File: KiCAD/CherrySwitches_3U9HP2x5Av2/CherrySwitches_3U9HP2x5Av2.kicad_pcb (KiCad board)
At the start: 2 copper layers, 45.4 x 128.5 mm, 14 parts, among them SW1 SW_SPST_MOUNT, SW10 SW_SPST_MOUNT, SW2 SW_SPST_MOUNT, SW3 SW_SPST_MOUNT, SW4 SW_SPST_MOUNT, SW5 SW_SPST_MOUNT, SW6 SW_SPST_MOUNT, SW7 SW_SPST_MOUNT, SW8 SW_SPST_MOUNT, SW9 SW_SPST_MOUNT

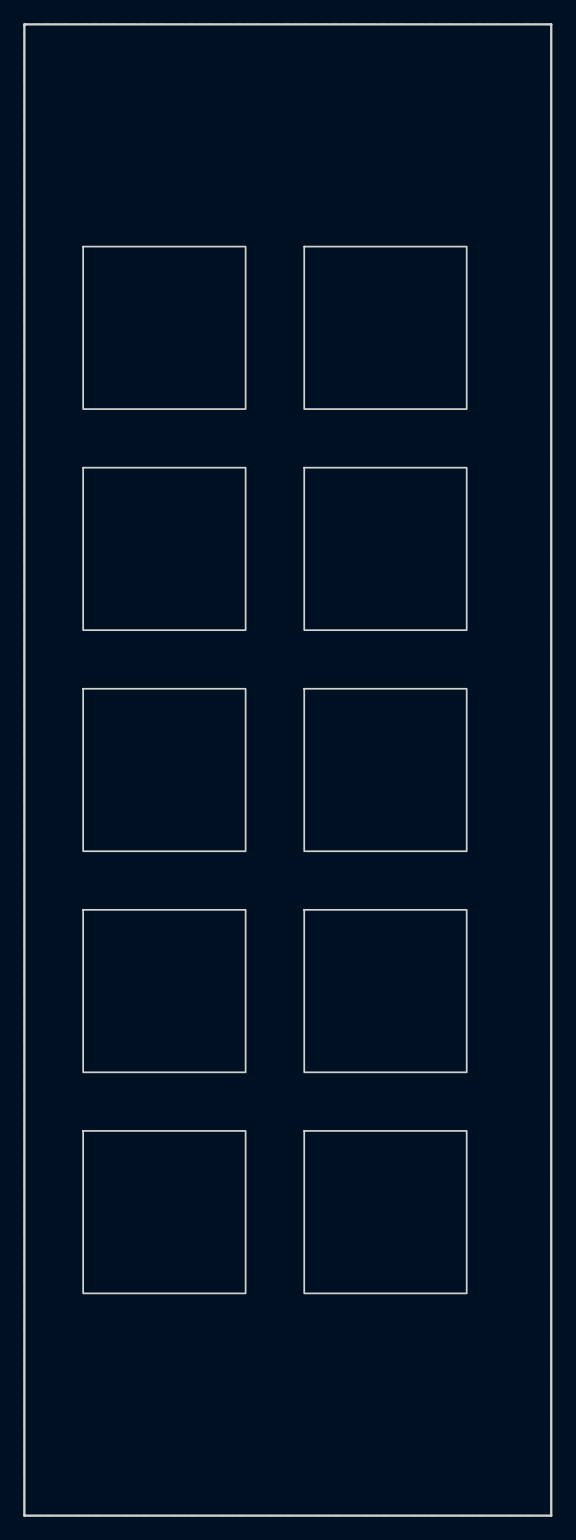
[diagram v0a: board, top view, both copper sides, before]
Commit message: updated all modules to use plated through-holes wherever possible
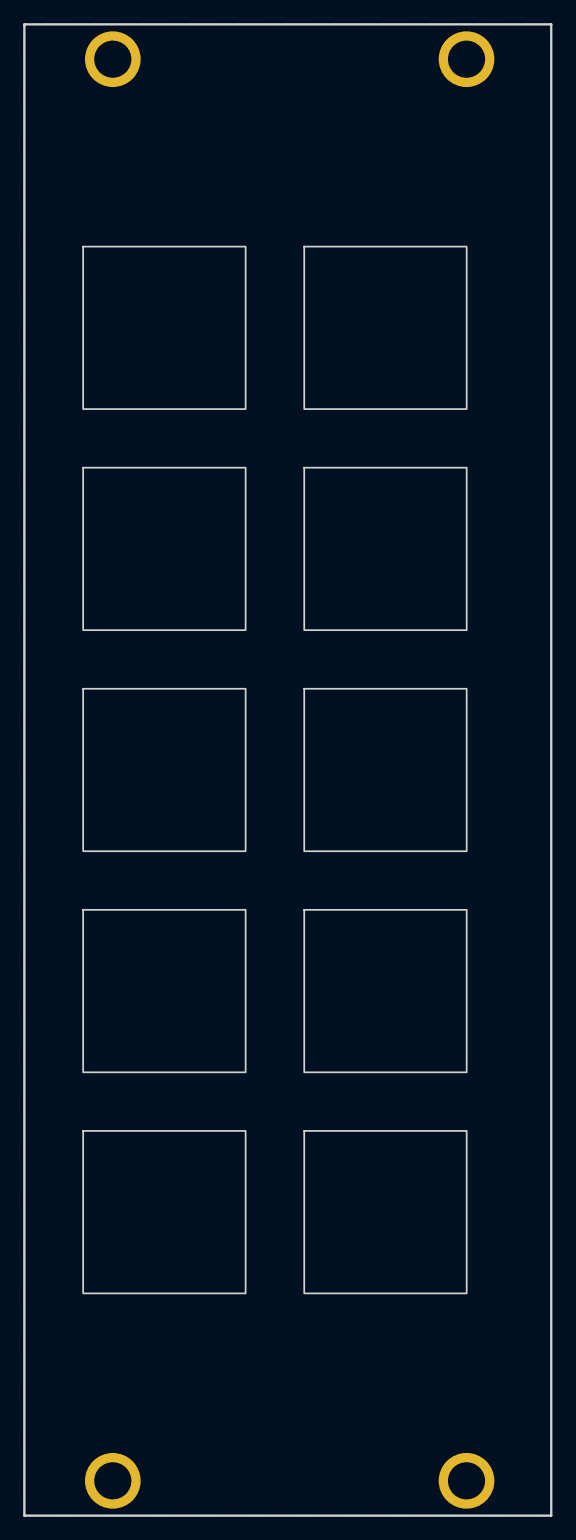
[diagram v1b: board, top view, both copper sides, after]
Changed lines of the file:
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@@
 			)
 		)
-		(pad "" np_thru_hole oval
+		(pad "" thru_hole circle
 			(at 0 0)
-			(size 4.34 3.2)
-			(drill oval 4.34 3.2)
+			(size 4.8 4.8)
+			(drill 3.2)
 			(layers "*.Cu" "*.Mask")
+			(remove_unused_layers no)
 		)
 		(embedded_fonts no)
@@
 			)
 		)
-		(pad "" np_thru_hole oval
+		(pad "" thru_hole circle
 			(at 0 0)
-			(size 4.34 3.2)
-			(drill oval 4.34 3.2)
+			(size 4.8 4.8)
+			(drill 3.2)
 			(layers "*.Cu" "*.Mask")
+			(remove_unused_layers no)
 		)
 		(embedded_fonts no)
@@
 			)
 		)
-		(pad "" np_thru_hole oval
+		(pad "" thru_hole circle
 			(at 0 0)
-			(size 4.34 3.2)
-			(drill oval 4.34 3.2)
+			(size 4.8 4.8)
+			(drill 3.2)
 			(layers "*.Cu" "*.Mask")
+			(remove_unused_layers no)
 		)
 		(embedded_fonts no)
@@
 			)
 		)
-		(pad "" np_thru_hole oval
+		(pad "" thru_hole circle
 			(at 0 0)
-			(size 4.34 3.2)
-			(drill oval 4.34 3.2)
+			(size 4.8 4.8)
+			(drill 3.2)
 			(layers "*.Cu" "*.Mask")
+			(remove_unused_layers no)
 		)
 		(embedded_fonts no)
